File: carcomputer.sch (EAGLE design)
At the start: 75 parts, among them IC1 LM358N, K1 351, K2 RT184012, K3 RT184012, Q1 BS170, Q5 TIP136, T1 BC618, T2 BC618, T3 BC618, T4 BC618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

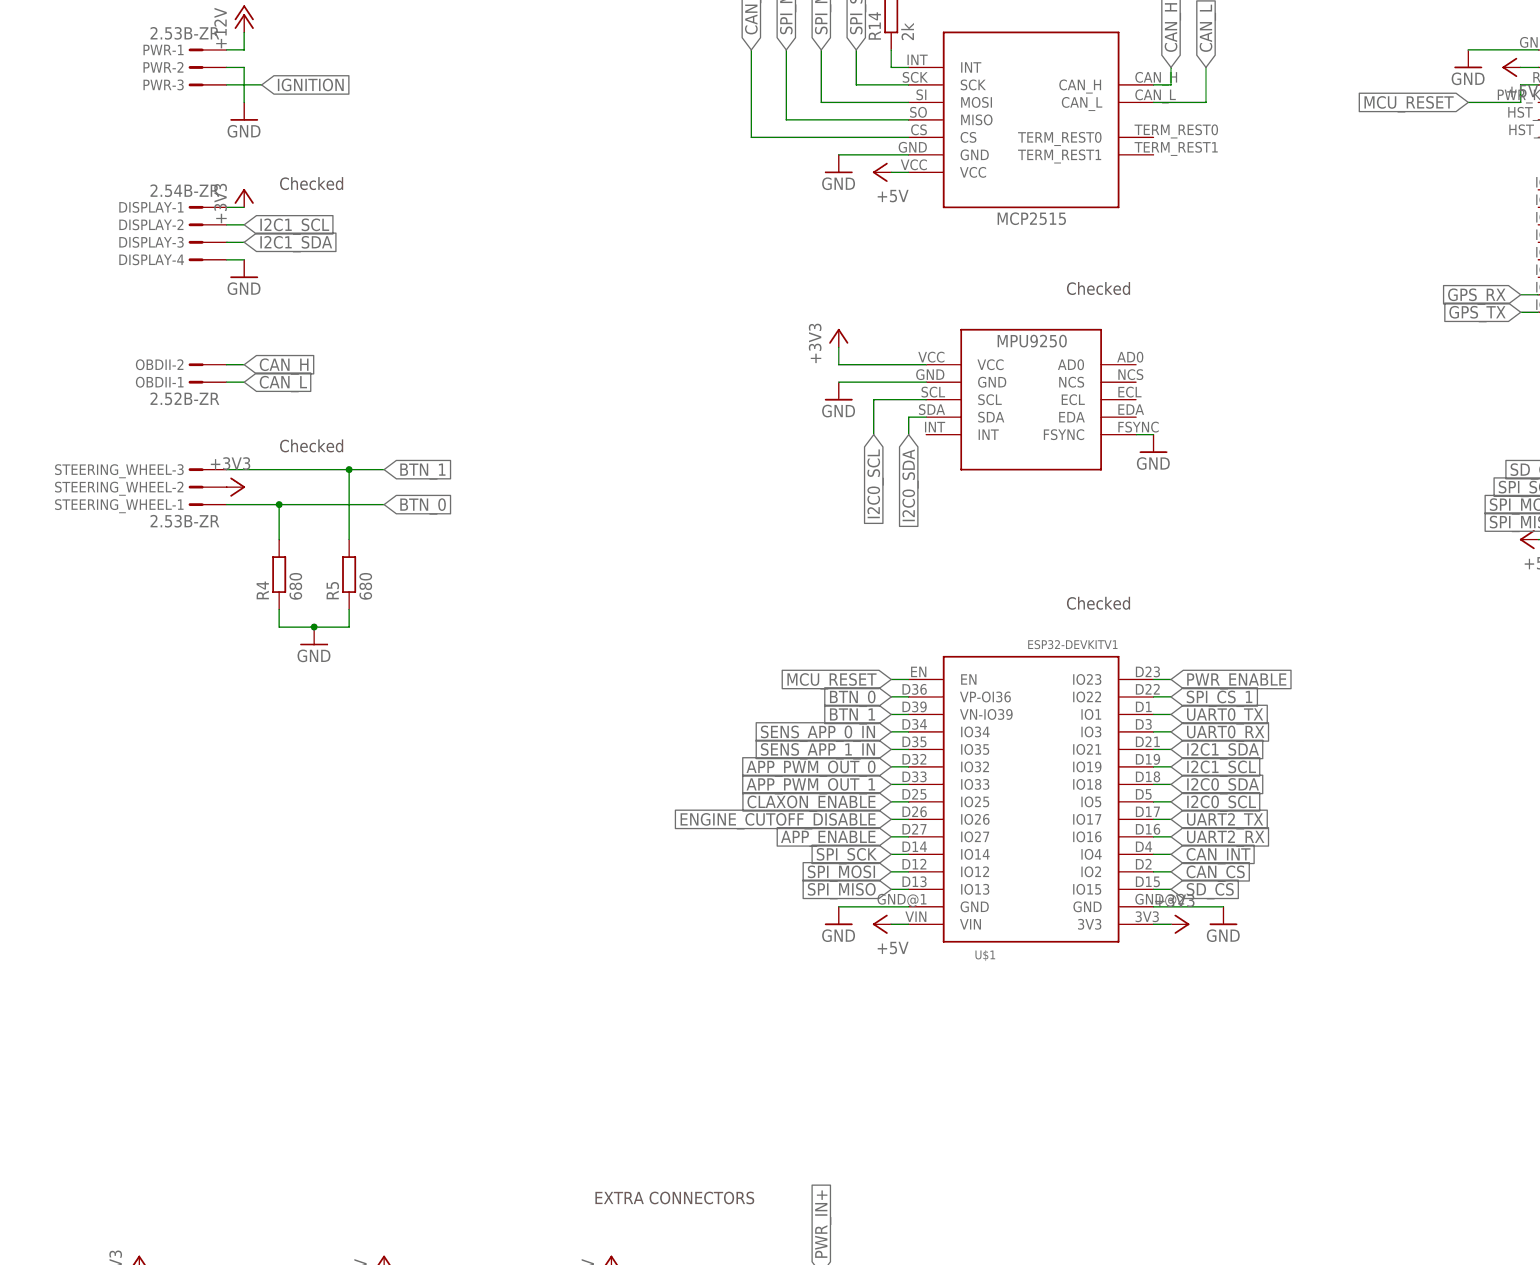
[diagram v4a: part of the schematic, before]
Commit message: Added pinheaders connection for CAN terminator resistors
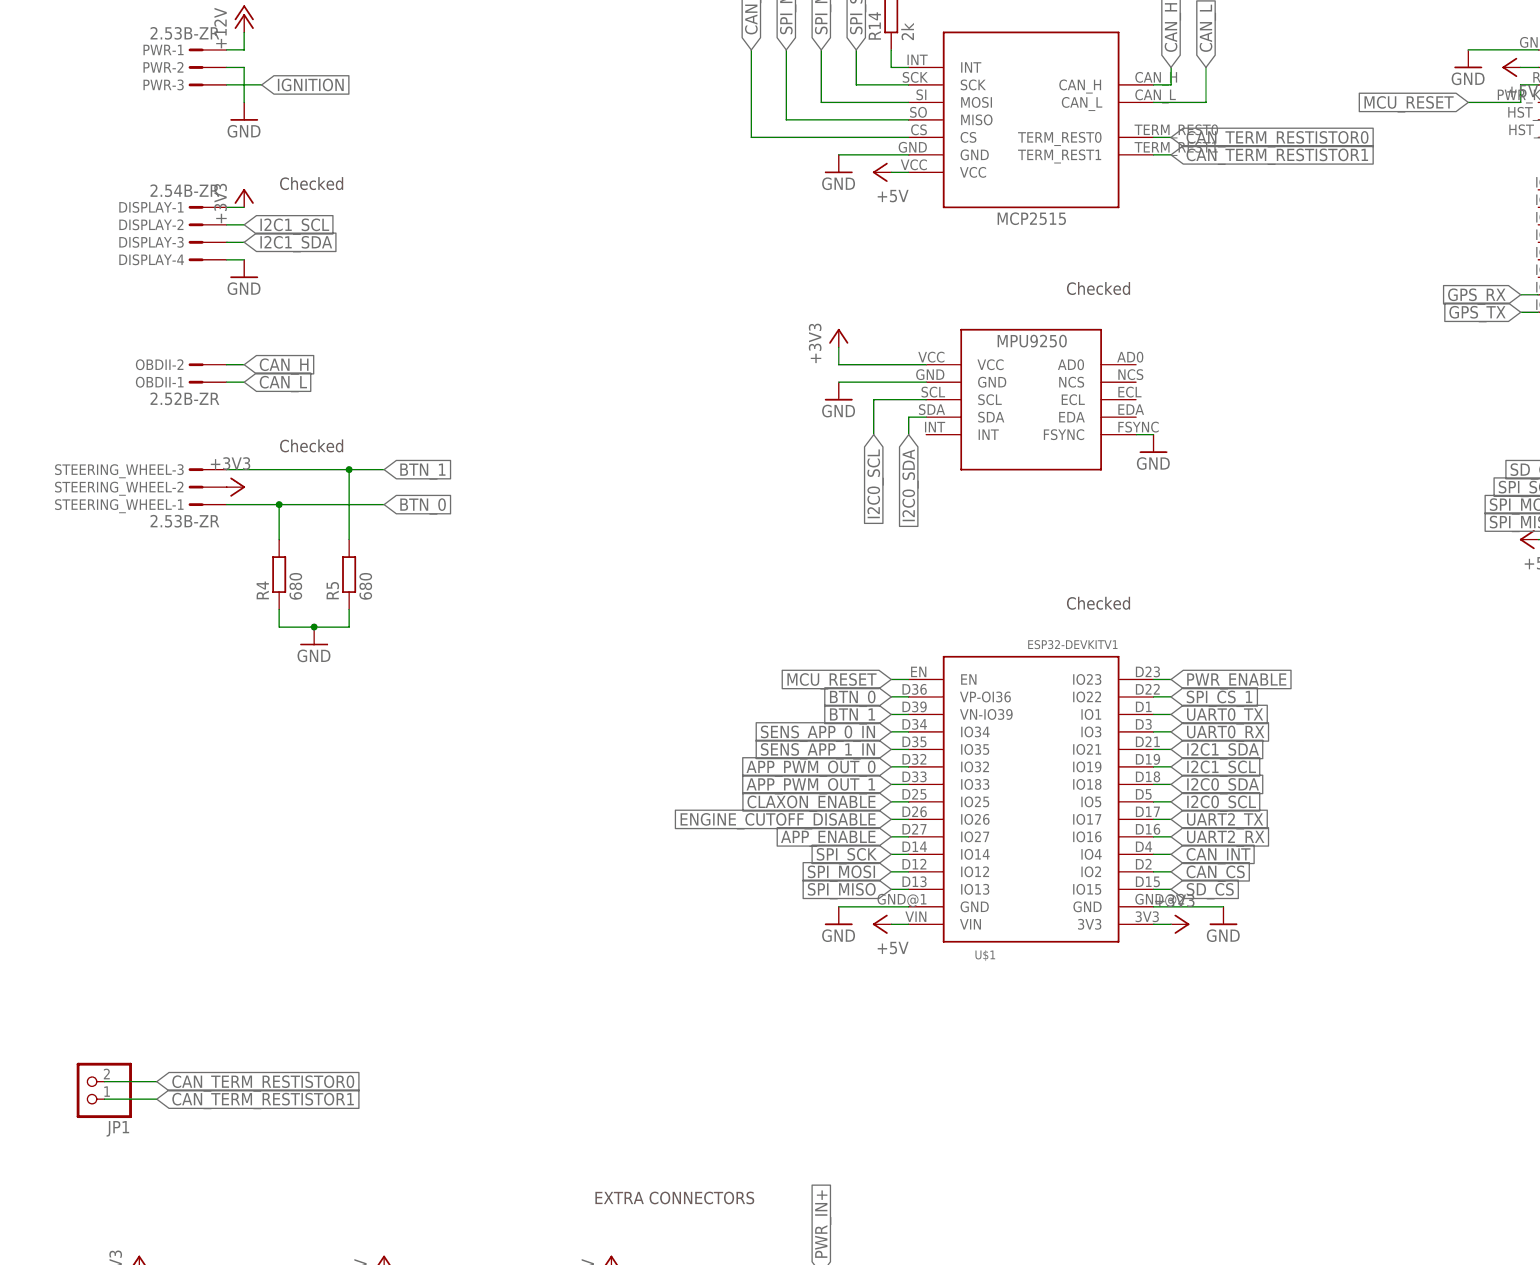
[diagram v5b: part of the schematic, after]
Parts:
- added JP1: (no value), pinhead:PINHD-1X2
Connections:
- new net CAN_TERM_RESTISTOR0: JP1.2, U$2.TERM_REST0
- new net CAN_TERM_RESTISTOR1: JP1.1, U$2.TERM_REST1
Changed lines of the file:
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@@
 <grid distance="0.1" unitdist="inch" unit="inch" style="lines" multiple="1" display="no" altdistance="0.01" altunitdist="inch" altunit="inch"/>
 <layers>
-<layer number="1" name="Top" color="4" fill="1" visible="yes" active="no"/>
-<layer number="16" name="Bottom" color="1" fill="1" visible="yes" active="no"/>
-<layer number="17" name="Pads" color="2" fill="1" visible="yes" active="no"/>
-<layer number="18" name="Vias" color="2" fill="1" visible="yes" active="no"/>
-<layer number="19" name="Unrouted" color="6" fill="1" visible="yes" active="no"/>
-<layer number="20" name="Dimension" color="24" fill="1" visible="yes" active="no"/>
-<layer number="21" name="tPlace" color="7" fill="1" visible="yes" active="no"/>
-<layer number="22" name="bPlace" color="7" fill="1" visible="yes" active="no"/>
-<layer number="23" name="tOrigins" color="15" fill="1" visible="yes" active="no"/>
-<layer number="24" name="bOrigins" color="15" fill="1" visible="yes" active="no"/>
-<layer number="25" name="tNames" color="7" fill="1" visible="yes" active="no"/>
-<layer number="26" name="bNames" color="7" fill="1" visible="yes" active="no"/>
-<layer number="27" name="tValues" color="7" fill="1" visible="yes" active="no"/>
-<layer number="28" name="bValues" color="7" fill="1" visible="yes" active="no"/>
+<layer number="1" name="Top" color="4" fill="1" visible="no" active="no"/>
+<layer number="16" name="Bottom" color="1" fill="1" visible="no" active="no"/>
+<layer number="17" name="Pads" color="2" fill="1" visible="no" active="no"/>
+<layer number="18" name="Vias" color="2" fill="1" visible="no" active="no"/>
+<layer number="19" name="Unrouted" color="6" fill="1" visible="no" active="no"/>
+<layer number="20" name="Dimension" color="24" fill="1" visible="no" active="no"/>
+<layer number="21" name="tPlace" color="7" fill="1" visible="no" active="no"/>
+<layer number="22" name="bPlace" color="7" fill="1" visible="no" active="no"/>
+<layer number="23" name="tOrigins" color="15" fill="1" visible="no" active="no"/>
+<layer number="24" name="bOrigins" color="15" fill="1" visible="no" active="no"/>
+<layer number="25" name="tNames" color="7" fill="1" visible="no" active="no"/>
+<layer number="26" name="bNames" color="7" fill="1" visible="no" active="no"/>
+<layer number="27" name="tValues" color="7" fill="1" visible="no" active="no"/>
+<layer number="28" name="bValues" color="7" fill="1" visible="no" active="no"/>
 <layer number="29" name="tStop" color="7" fill="3" visible="no" active="no"/>
 <layer number="30" name="bStop" color="7" fill="6" visible="no" active="no"/>
@@
 <layer number="35" name="tGlue" color="7" fill="4" visible="no" active="no"/>
 <layer number="36" name="bGlue" color="7" fill="5" visible="no" active="no"/>
-<layer number="37" name="tTest" color="7" fill="1" visible="yes" active="no"/>
-<layer number="38" name="bTest" color="7" fill="1" visible="yes" active="no"/>
+<layer number="37" name="tTest" color="7" fill="1" visible="no" active="no"/>
+<layer number="38" name="bTest" color="7" fill="1" visible="no" active="no"/>
 <layer number="39" name="tKeepout" color="4" fill="11" visible="no" active="no"/>
 <layer number="40" name="bKeepout" color="1" fill="11" visible="no" active="no"/>
@@
 <layer number="44" name="Drills" color="7" fill="1" visible="no" active="no"/>
 <layer number="45" name="Holes" color="7" fill="1" visible="no" active="no"/>
-<layer number="46" name="Milling" color="3" fill="1" visible="yes" active="no"/>
-<layer number="47" name="Measures" color="7" fill="1" visible="yes" active="no"/>
-<layer number="48" name="Document" color="7" fill="1" visible="yes" active="no"/>
-<layer number="49" name="Reference" color="7" fill="1" visible="yes" active="no"/>
-<layer number="50" name="dxf" color="7" fill="1" visible="yes" active="no"/>
-<layer number="51" name="tDocu" color="7" fill="1" visible="yes" active="no"/>
-<layer number="52" name="bDocu" color="7" fill="1" visible="yes" active="no"/>
+<layer number="46" name="Milling" color="3" fill="1" visible="no" active="no"/>
+<layer number="47" name="Measures" color="7" fill="1" visible="no" active="no"/>
+<layer number="48" name="Document" color="7" fill="1" visible="no" active="no"/>
+<layer number="49" name="Reference" color="7" fill="1" visible="no" active="no"/>
+<layer number="50" name="dxf" color="7" fill="1" visible="no" active="no"/>
+<layer number="51" name="tDocu" color="7" fill="1" visible="no" active="no"/>
+<layer number="52" name="bDocu" color="7" fill="1" visible="no" active="no"/>
 <layer number="88" name="SimResults" color="9" fill="1" visible="yes" active="yes"/>
 <layer number="89" name="SimProbes" color="9" fill="1" visible="yes" active="yes"/>
@@
 <part name="X1" library="con-jst-custom" deviceset="?2B-ZR" device="2.5"/>
 <part name="X2" library="con-jst-custom" deviceset="?2B-ZR" device="2.5"/>
+<part name="JP1" library="pinhead" library_urn="urn:adsk.eagle:library:325" deviceset="PINHD-1X2" device="" package3d_urn="urn:adsk.eagle:package:22435/2"/>
 </parts>
 <sheets>
@@
 <attribute name="NAME" x="131.064" y="107.442" size="1.524" layer="95" rot="R180"/>
 </instance>
+<instance part="JP1" gate="G$1" x="-182.88" y="-5.08" smashed="yes" rot="R180">
+<attribute name="NAME" x="-176.53" y="-10.795" size="1.778" layer="95" rot="R180"/>
+<attribute name="VALUE" x="-176.53" y="0" size="1.778" layer="96" rot="R180"/>
+</instance>
 </instances>
 <busses>
@@
 </segment>
 </net>
+<net name="CAN_TERM_RESTISTOR0" class="0">
+<segment>
+<pinref part="U$2" gate="G$1" pin="TERM_REST0"/>
+<wire x1="-27.94" y1="132.08" x2="-25.4" y2="132.08" width="0.1524" layer="91"/>
+<label x="-25.4" y="132.08" size="1.778" layer="95" xref="yes"/>
+</segment>
+<segment>
+<pinref part="JP1" gate="G$1" pin="2"/>
+<wire x1="-180.34" y1="-5.08" x2="-172.72" y2="-5.08" width="0.1524" layer="91"/>
+<label x="-172.72" y="-5.08" size="1.778" layer="95" xref="yes"/>
+</segment>
+</net>
+<net name="CAN_TERM_RESTISTOR1" class="0">
+<segment>
+<pinref part="U$2" gate="G$1" pin="TERM_REST1"/>
+<wire x1="-27.94" y1="129.54" x2="-25.4" y2="129.54" width="0.1524" layer="91"/>
+<label x="-25.4" y="129.54" size="1.778" layer="95" xref="yes"/>
+</segment>
+<segment>
+<pinref part="JP1" gate="G$1" pin="1"/>
+<wire x1="-180.34" y1="-7.62" x2="-172.72" y2="-7.62" width="0.1524" layer="91"/>
+<label x="-172.72" y="-7.62" size="1.778" layer="95" xref="yes"/>
+</segment>
+</net>

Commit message: Placed labels next to components. Rearranged silkscreen. Improved vias
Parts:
- renumbered JP1 to CAN_TERM_RESISTOR, S1 to RESET
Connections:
- net +3V3: now also DISPLAY-4.1; no longer DISPLAY-1.1
- net GND: now also DISPLAY-1.1; no longer DISPLAY-4.1
- net I2C1_SCL: now also DISPLAY-3.1; no longer DISPLAY-2.1
- net I2C1_SDA: now also DISPLAY-2.1; no longer DISPLAY-3.1
- net N$19: now also ENGINE_CUTOFF_CONN-2.KL; no longer ENGINE_CUTOFF_CONN-1.KL
- net N$20: now also ENGINE_CUTOFF_CONN-1.KL; no longer ENGINE_CUTOFF_CONN-2.KL
- net N$27: now also CLAXON_CONN-2.KL; no longer CLAXON_CONN-1.KL
- net N$28: now also CLAXON_CONN-1.KL; no longer CLAXON_CONN-2.KL
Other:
- moved on the sheet: CLAXON_CONN-1, CLAXON_CONN-2, DISPLAY-1, DISPLAY-2, DISPLAY-3, DISPLAY-4, ENGINE_CUTOFF_CONN-1, ENGINE_CUTOFF_CONN-2

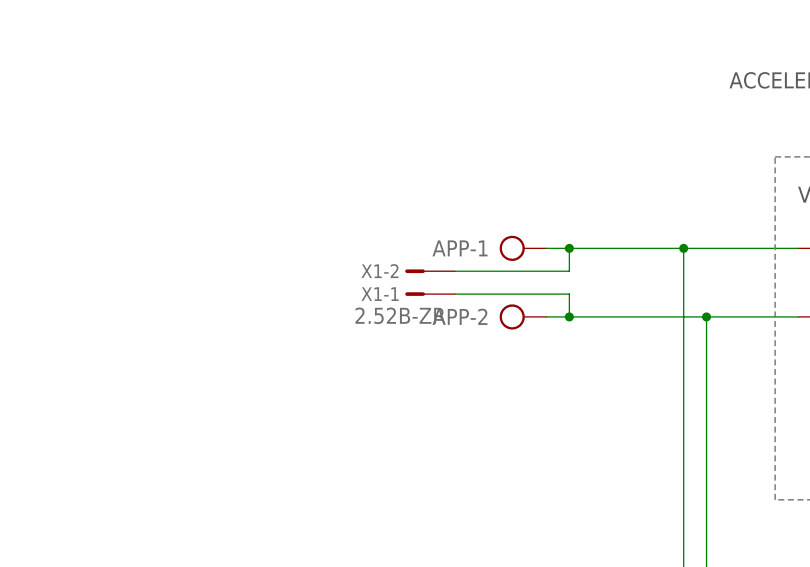
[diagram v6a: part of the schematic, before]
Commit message: Updated silkscreen
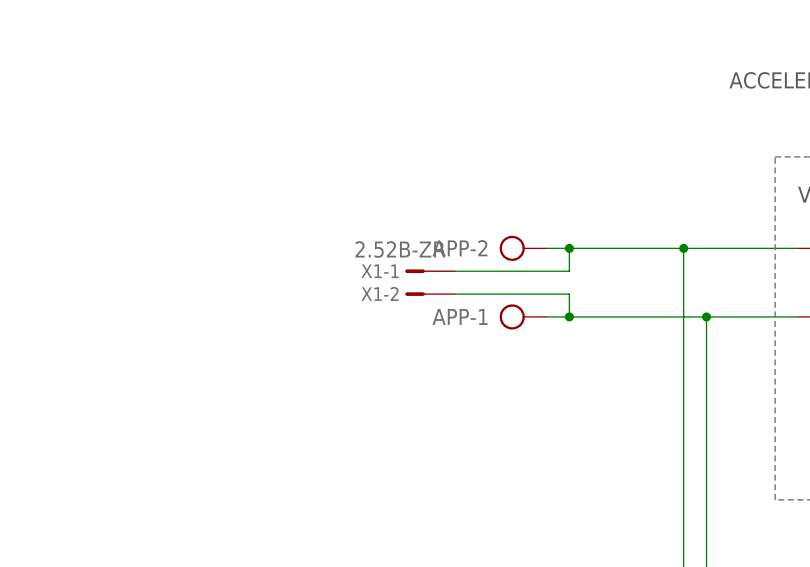
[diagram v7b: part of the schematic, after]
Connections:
- net APP_0_IN: now also APP-2.KL, X1-1.1; no longer APP-1.KL, X1-2.1
- net APP_1_IN: now also APP-1.KL, X1-2.1; no longer APP-2.KL, X1-1.1
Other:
- moved on the sheet: APP-1, APP-2, X1-1, X1-2
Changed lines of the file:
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@@
 <attribute name="VALUE" x="135.89" y="108.077" size="1.778" layer="96"/>
 </instance>
-<instance part="APP" gate="-1" x="139.7" y="165.1" smashed="yes">
-<attribute name="NAME" x="138.43" y="165.989" size="1.778" layer="95" rot="R180"/>
-</instance>
-<instance part="APP" gate="-2" x="139.7" y="157.48" smashed="yes">
-<attribute name="NAME" x="138.43" y="158.369" size="1.778" layer="95" rot="R180"/>
-<attribute name="VALUE" x="135.89" y="153.797" size="1.778" layer="96"/>
+<instance part="APP" gate="-1" x="139.7" y="157.48" smashed="yes" rot="MR180">
+<attribute name="NAME" x="138.43" y="156.591" size="1.778" layer="95" rot="MR0"/>
+</instance>
+<instance part="APP" gate="-2" x="139.7" y="165.1" smashed="yes" rot="MR180">
+<attribute name="NAME" x="138.43" y="164.211" size="1.778" layer="95" rot="MR0"/>
+<attribute name="VALUE" x="135.89" y="168.783" size="1.778" layer="96" rot="MR180"/>
 </instance>
 <instance part="K1" gate="1" x="157.48" y="68.58" smashed="yes" rot="R90">
@@
 <attribute name="PART" x="154.94" y="-167.64" size="1.778" layer="95" rot="R270"/>
 </instance>
-<instance part="X1" gate="-1" x="129.54" y="160.02" smashed="yes" rot="R180">
-<attribute name="NAME" x="128.524" y="160.782" size="1.524" layer="95" rot="R180"/>
-<attribute name="VALUE" x="133.604" y="158.496" size="1.778" layer="96" rot="R180"/>
-</instance>
-<instance part="X1" gate="-2" x="129.54" y="162.56" smashed="yes" rot="R180">
-<attribute name="NAME" x="128.524" y="163.322" size="1.524" layer="95" rot="R180"/>
+<instance part="X1" gate="-1" x="129.54" y="162.56" smashed="yes" rot="MR0">
+<attribute name="NAME" x="128.524" y="161.798" size="1.524" layer="95" rot="MR0"/>
+<attribute name="VALUE" x="133.604" y="164.084" size="1.778" layer="96" rot="MR0"/>
+</instance>
+<instance part="X1" gate="-2" x="129.54" y="160.02" smashed="yes" rot="MR0">
+<attribute name="NAME" x="128.524" y="159.258" size="1.524" layer="95" rot="MR0"/>
 </instance>
 <instance part="X2" gate="-1" x="132.08" y="104.14" smashed="yes" rot="R180">
@@
 <net name="APP_0_IN" class="0">
 <segment>
-<pinref part="APP" gate="-1" pin="KL"/>
-<wire x1="144.78" y1="165.1" x2="147.32" y2="165.1" width="0.1524" layer="91"/>
 <pinref part="K1" gate="3" pin="O"/>
-<wire x1="147.32" y1="165.1" x2="160.02" y2="165.1" width="0.1524" layer="91"/>
 <wire x1="160.02" y1="116.84" x2="160.02" y2="165.1" width="0.1524" layer="91"/>
 <pinref part="R11" gate="G$1" pin="2"/>
 <wire x1="160.02" y1="165.1" x2="172.72" y2="165.1" width="0.1524" layer="91"/>
+<pinref part="APP" gate="-2" pin="KL"/>
+<wire x1="144.78" y1="165.1" x2="147.32" y2="165.1" width="0.1524" layer="91"/>
+<wire x1="147.32" y1="162.56" x2="147.32" y2="165.1" width="0.1524" layer="91"/>
+<pinref part="X1" gate="-1" pin="1"/>
+<wire x1="134.62" y1="162.56" x2="147.32" y2="162.56" width="0.1524" layer="91"/>
+<wire x1="147.32" y1="165.1" x2="160.02" y2="165.1" width="0.1524" layer="91"/>
+<junction x="147.32" y="165.1"/>
 <junction x="160.02" y="165.1"/>
-<pinref part="X1" gate="-2" pin="1"/>
-<wire x1="134.62" y1="162.56" x2="147.32" y2="162.56" width="0.1524" layer="91"/>
-<wire x1="147.32" y1="162.56" x2="147.32" y2="165.1" width="0.1524" layer="91"/>
-<junction x="147.32" y="165.1"/>
 </segment>
 </net>
 <net name="APP_1_IN" class="0">
 <segment>
-<pinref part="APP" gate="-2" pin="KL"/>
-<wire x1="144.78" y1="157.48" x2="147.32" y2="157.48" width="0.1524" layer="91"/>
 <pinref part="K1" gate="2" pin="O"/>
-<wire x1="147.32" y1="157.48" x2="162.56" y2="157.48" width="0.1524" layer="91"/>
 <wire x1="160.02" y1="101.6" x2="162.56" y2="101.6" width="0.1524" layer="91"/>
 <wire x1="162.56" y1="101.6" x2="162.56" y2="157.48" width="0.1524" layer="91"/>
 <pinref part="R9" gate="G$1" pin="2"/>
 <wire x1="162.56" y1="157.48" x2="172.72" y2="157.48" width="0.1524" layer="91"/>
+<pinref part="APP" gate="-1" pin="KL"/>
+<wire x1="144.78" y1="157.48" x2="147.32" y2="157.48" width="0.1524" layer="91"/>
+<wire x1="147.32" y1="160.02" x2="147.32" y2="157.48" width="0.1524" layer="91"/>
+<pinref part="X1" gate="-2" pin="1"/>
+<wire x1="134.62" y1="160.02" x2="147.32" y2="160.02" width="0.1524" layer="91"/>
+<wire x1="147.32" y1="157.48" x2="162.56" y2="157.48" width="0.1524" layer="91"/>
+<junction x="147.32" y="157.48"/>
 <junction x="162.56" y="157.48"/>
-<pinref part="X1" gate="-1" pin="1"/>
-<wire x1="134.62" y1="160.02" x2="147.32" y2="160.02" width="0.1524" layer="91"/>
-<wire x1="147.32" y1="160.02" x2="147.32" y2="157.48" width="0.1524" layer="91"/>
-<junction x="147.32" y="157.48"/>
-</segment>
-</net>
+</segment>
+</net>
